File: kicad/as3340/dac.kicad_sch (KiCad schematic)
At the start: 21 parts, among them U12 TL074, U13 LM4040AIM3-2.5, U14 AD5328

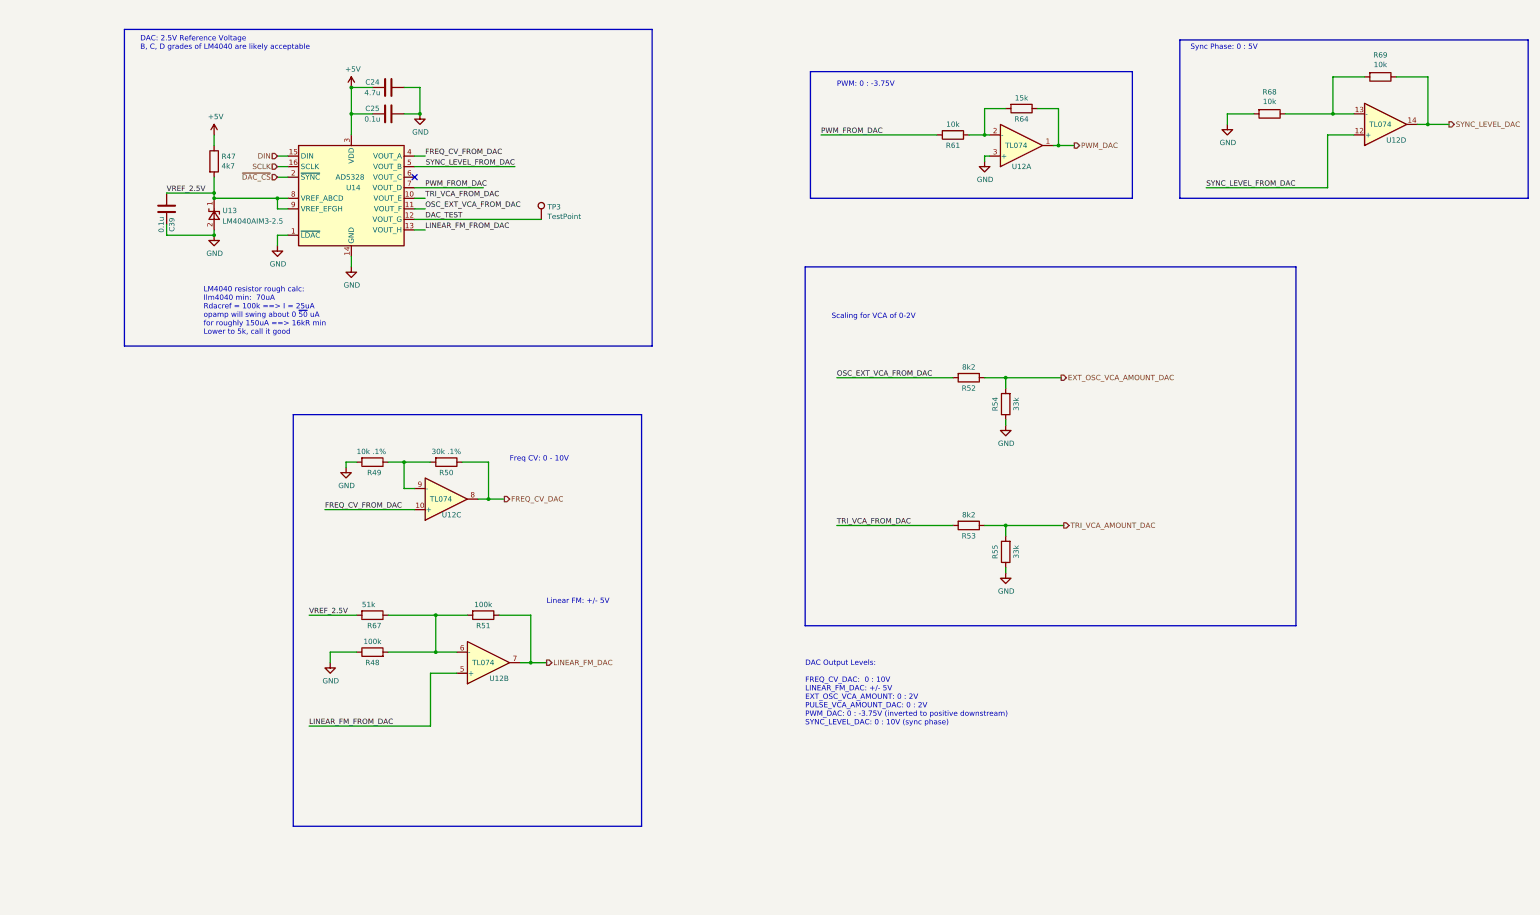
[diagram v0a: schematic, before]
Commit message: change DAC Freq CV to 0-6.5V; add lowpass caps on DAC lines; fix SOT-23 pinout
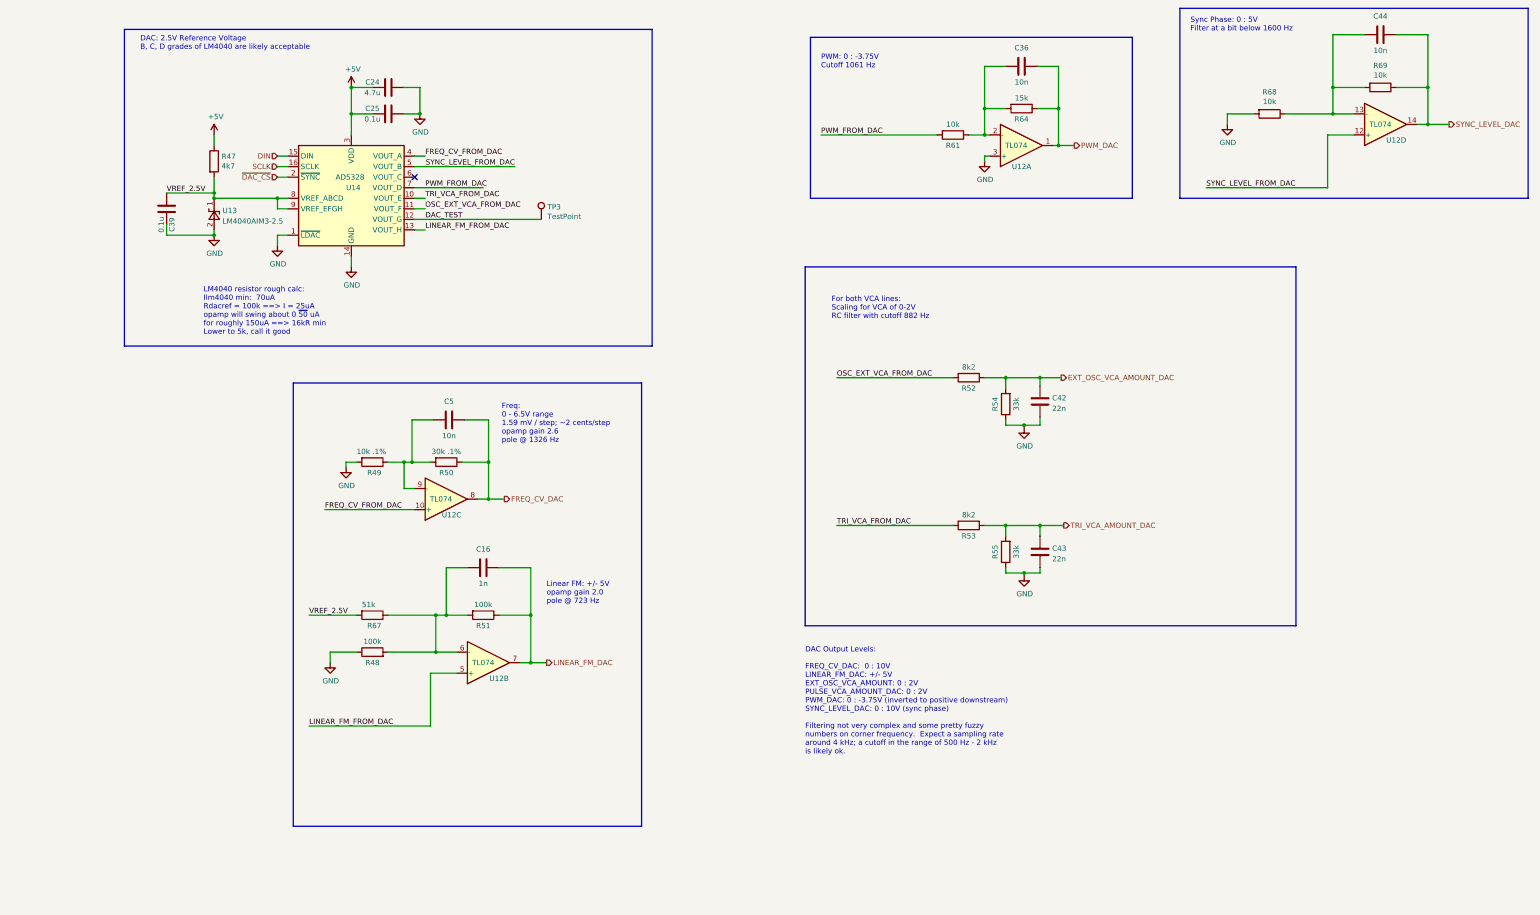
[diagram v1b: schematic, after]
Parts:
- added C16: 1n, Capacitor_SMD:C_0603_1608Metric, symbol Device:C
- added C36, C44, C5: 10n, Capacitor_SMD:C_0603_1608Metric, symbol Device:C
- added C42, C43: 22n, Capacitor_SMD:C_0603_1608Metric, symbol Device:C
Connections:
- net EXT_OSC_VCA_AMOUNT_DAC: now also C42.1
- net FREQ_CV_DAC: now also C5.2
- net GND: now also C42.2, C43.2
- net LINEAR_FM_DAC: now also C16.2
- net PWM_DAC: now also C36.2
- net SYNC_LEVEL_DAC: now also C44.2
- net TRI_VCA_AMOUNT_DAC: now also C43.1
- net at R49.1, R50.2, U12.9 (-): now also C5.1
- net at R48.2, R51.2, R67.1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: now also C16.1
- net at R61.1, R64.2, U12.2 (-): now also C36.1
- net at R68.1, R69.2, U12.13 (-): now also C44.1
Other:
- note added: "DAC Output Levels: FREQ_CV_DAC: 0 : 10V LINEAR_FM_DAC: +/- 5V EXT_OSC_VCA_AMOUNT: 0 : 2V PULSE_VCA_AMOUNT_DAC: 0 : 2V PWM_DAC: 0 : -3.75V (inverted to positive downstream) SYNC_LEVEL_DAC: 0 : 10V (sync phase) Filtering not very complex and some pretty fuzzy numbers on corner frequency. Expect a sampling rate around 4 kHz; a cutoff in the range of 500 Hz - 2 kHz is likely ok."
- note added: "For both VCA lines: Scaling for VCA of 0-2V RC filter with cutoff 882 Hz"
- note added: "Freq: 0 - 6.5V range 1.59 mV / step; ~2 cents/step opamp gain 2.6 pole @ 1326 Hz"
- note added: "Linear FM: +/- 5V opamp gain 2.0 pole @ 723 Hz"
- note added: "PWM: 0 : -3.75V Cutoff 1061 Hz"
- note added: "Sync Phase: 0 : 5V Filter at a bit below 1600 Hz"
- note removed: "DAC Output Levels: FREQ_CV_DAC: 0 : 10V LINEAR_FM_DAC: +/- 5V EXT_OSC_VCA_AMOUNT: 0 : 2V PULSE_VCA_AMOUNT_DAC: 0 : 2V PWM_DAC: 0 : -3.75V (inverted to positive downstream) SYNC_LEVEL_DAC: 0 : 10V (sync phase)"
- note removed: "Freq CV: 0 - 10V"
- note removed: "Linear FM: +/- 5V"
- note removed: "PWM: 0 : -3.75V"
- note removed: "Scaling for VCA of 0-2V"
- note removed: "Sync Phase: 0 : 5V"
- moved on the sheet: R69

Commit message: gerbers and build artifacts produced
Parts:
- U13: LCSC Part C131939 -> C460725
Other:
- note added: "DAC: 2.5V Reference Voltage B, C, D grades of LM4040 are likely good 'nuff"
- note removed: "DAC: 2.5V Reference Voltage B, C, D grades of LM4040 are likely acceptable"
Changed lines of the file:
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@@
     (effects (font (size 1.27 1.27)) (justify left bottom))
   )
-  (text "DAC: 2.5V Reference Voltage\nB, C, D grades of LM4040 are likely acceptable"
+  (text "DAC: 2.5V Reference Voltage\nB, C, D grades of LM4040 are likely good 'nuff"
     (at 49.53 38.1 0)
     (effects (font (size 1.27 1.27)) (justify left bottom))
@@
       (effects (font (size 1.27 1.27) italic) hide)
     )
-    (property "LCSC Part" "C131939" (id 4) (at 67.31 77.47 90)
-      (effects (font (size 1.27 1.27)) hide)
-    )
+    (property "LCSC Part" "C460725" (id 4) (at 67.31 77.47 90)
+      (effects (font (size 1.27 1.27)) hide)
+    )

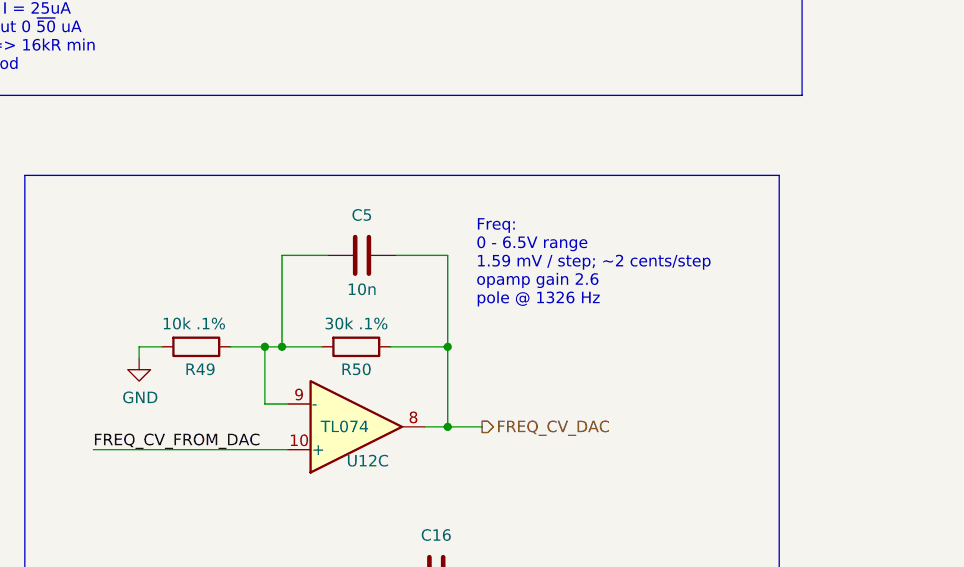
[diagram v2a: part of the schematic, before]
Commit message: changed output scaling; CV freq range; removed comp output
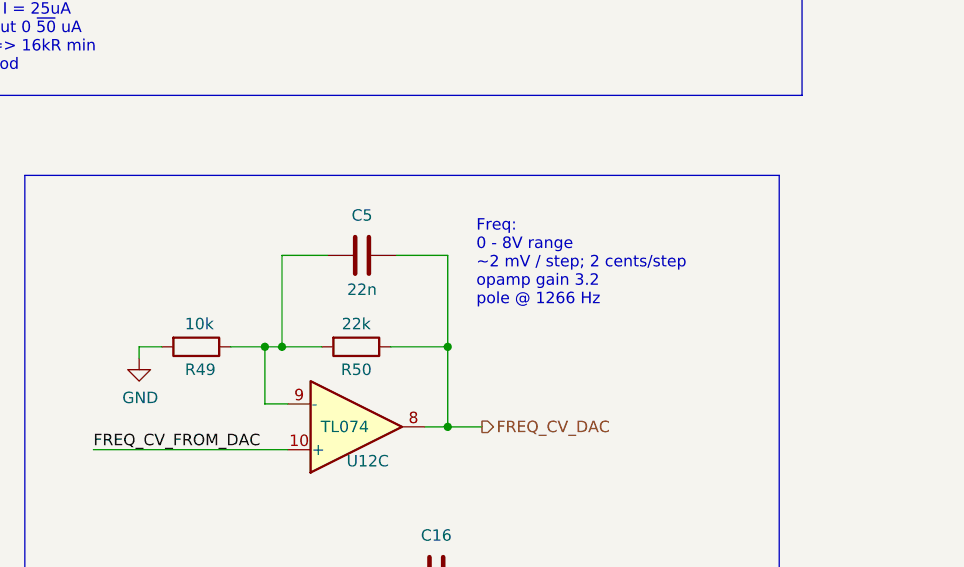
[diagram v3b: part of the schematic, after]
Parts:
- C5: value 10n -> 22n; LCSC Part C57112 -> C21122
- R49: value 10k .1% -> 10k
- R50: value 30k .1% -> 22k; LCSC Part C22984 -> C31850
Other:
- note added: "Freq: 0 - 8V range ~2 mV / step; 2 cents/step opamp gain 3.2 pole @ 1266 Hz"
- note removed: "Freq: 0 - 6.5V range 1.59 mV / step; ~2 cents/step opamp gain 2.6 pole @ 1326 Hz"
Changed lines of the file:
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@@
     (effects (font (size 1.27 1.27)) (justify left bottom))
   )
-  (text "Freq:\n0 - 6.5V range\n1.59 mV / step; ~2 cents/step\nopamp gain 2.6\npole @ 1326 Hz"
+  (text "Freq:\n0 - 8V range\n~2 mV / step; 2 cents/step\nopamp gain 3.2\npole @ 1266 Hz"
     (at 136.525 132.715 0)
     (effects (font (size 1.27 1.27)) (justify left bottom))
@@
     (in_bom yes) (on_board yes)
     (property "Reference" "R50" (id 0) (at 123.19 139.7 90))
-    (property "Value" "30k .1%" (id 1) (at 123.19 134.62 90))
+    (property "Value" "22k" (id 1) (at 123.19 134.62 90))
     (property "Footprint" "Resistor_SMD:R_0603_1608Metric" (id 2) (at 123.19 135.382 90)
       (effects (font (size 1.27 1.27)) hide)
@@
       (effects (font (size 1.27 1.27)) hide)
     )
-    (property "LCSC Part" "C22984" (id 4) (at 123.19 137.16 0)
+    (property "LCSC Part" "C31850" (id 4) (at 123.19 137.16 0)
       (effects (font (size 1.27 1.27)) hide)
     )
@@
       (effects (font (size 1.27 1.27)) (justify left))
     )
-    (property "Value" "10k .1%" (id 1) (at 101.6 134.62 90)
+    (property "Value" "10k" (id 1) (at 104.14 134.62 90)
       (effects (font (size 1.27 1.27)) (justify left))
     )
@@
     (in_bom yes) (on_board yes)
     (property "Reference" "C5" (id 0) (at 123.825 122.555 90))
-    (property "Value" "10n" (id 1) (at 123.825 130.81 90))
+    (property "Value" "22n" (id 1) (at 123.825 130.81 90))
     (property "Footprint" "Capacitor_SMD:C_0603_1608Metric" (id 2) (at 127.635 126.0348 0)
       (effects (font (size 1.27 1.27)) hide)
@@
       (effects (font (size 1.27 1.27)) hide)
     )
-    (property "LCSC Part" "C57112" (id 5) (at 123.825 127 0)
-      (effects (font (size 1.27 1.27)) hide)
-    )
+    (property "LCSC Part" "C21122" (id 5) (at 123.825 127 0)
+      (effects (font (size 1.27 1.27)) hide)
+    )
